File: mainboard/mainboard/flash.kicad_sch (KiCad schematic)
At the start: 5 parts

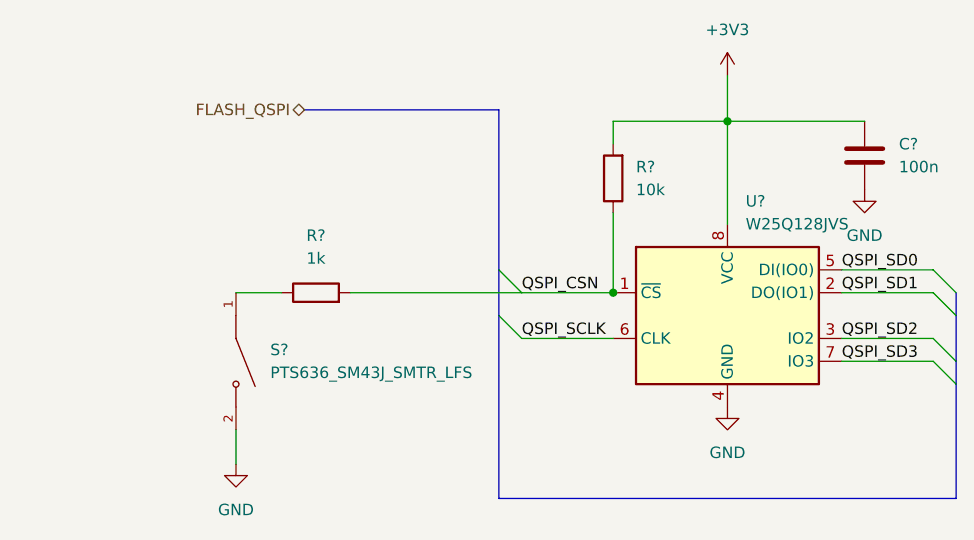
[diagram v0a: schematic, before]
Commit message: Fixing labels
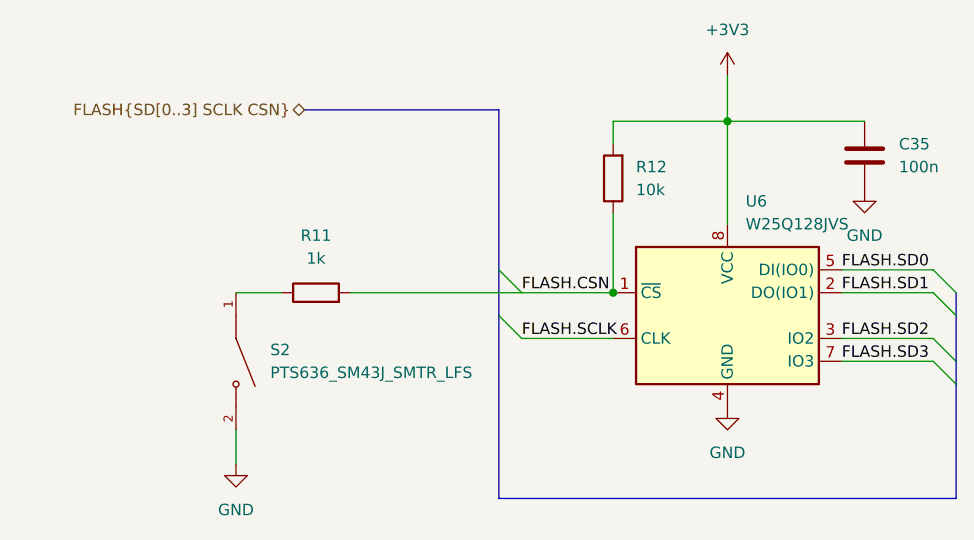
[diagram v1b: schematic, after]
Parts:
- gave numbers to parts that had none: 5
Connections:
- net QSPI_CSN renamed FLASH.CSN
- net QSPI_SCLK renamed FLASH.SCLK
- net QSPI_SD0 renamed FLASH.SD0
- net QSPI_SD1 renamed FLASH.SD1
- net QSPI_SD2 renamed FLASH.SD2
- net QSPI_SD3 renamed FLASH.SD3
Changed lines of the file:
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@@
     (stroke (width 0) (type default) (color 0 0 0 0))
   )
-  (label "QSPI_CSN" (at 123.19 81.28 0)
+  (label "FLASH.CSN" (at 123.19 81.28 0)
     (effects (font (size 1.27 1.27)) (justify left bottom))
   )
-  (label "QSPI_SCLK" (at 123.19 86.36 0)
+  (label "FLASH.SCLK" (at 123.19 86.36 0)
     (effects (font (size 1.27 1.27)) (justify left bottom))
   )
-  (label "QSPI_SD3" (at 158.75 88.9 0)
+  (label "FLASH.SD3" (at 158.75 88.9 0)
     (effects (font (size 1.27 1.27)) (justify left bottom))
   )
-  (label "QSPI_SD0" (at 158.75 78.74 0)
+  (label "FLASH.SD0" (at 158.75 78.74 0)
     (effects (font (size 1.27 1.27)) (justify left bottom))
   )
-  (label "QSPI_SD1" (at 158.75 81.28 0)
+  (label "FLASH.SD1" (at 158.75 81.28 0)
     (effects (font (size 1.27 1.27)) (justify left bottom))
   )
-  (label "QSPI_SD2" (at 158.75 86.36 0)
+  (label "FLASH.SD2" (at 158.75 86.36 0)
     (effects (font (size 1.27 1.27)) (justify left bottom))
   )
-  (hierarchical_label "FLASH_QSPI" (shape bidirectional) (at 99.06 60.96 180)
+  (hierarchical_label "FLASH{SD[0..3] SCLK CSN}" (shape bidirectional) (at 99.06 60.96 180)
     (effects (font (size 1.27 1.27)) (justify right))
   )
   (symbol (lib_id "Device:R") (at 100.33 81.28 90) (unit 1)
     (in_bom yes) (on_board yes) (fields_autoplaced)
-    (property "Reference" "R?" (id 0) (at 100.33 74.93 90))
+    (property "Reference" "R11" (id 0) (at 100.33 74.93 90))
     (property "Value" "1k" (id 1) (at 100.33 77.47 90))
     (property "Footprint" "Resistor_SMD:R_0402_1005Metric_Pad0.72x0.64mm_HandSolder" (id 2) (at 100.33 83.058 90)
@@
   (symbol (lib_id "Device:R") (at 133.35 68.58 180) (unit 1)
     (in_bom yes) (on_board yes) (fields_autoplaced)
-    (property "Reference" "R?" (id 0) (at 135.89 67.3099 0)
+    (property "Reference" "R12" (id 0) (at 135.89 67.3099 0)
       (effects (font (size 1.27 1.27)) (justify right))
     )
@@
   (symbol (lib_id "power:GND") (at 146.05 93.98 0) (unit 1)
     (in_bom yes) (on_board yes) (fields_autoplaced)
-    (property "Reference" "#PWR?" (id 0) (at 146.05 100.33 0)
+    (property "Reference" "#PWR044" (id 0) (at 146.05 100.33 0)
       (effects (font (size 1.27 1.27)) hide)
     )
@@
   (symbol (lib_id "PTS636_SM43J_SMTR_LFS:PTS636_SM43J_SMTR_LFS") (at 91.44 88.9 270) (unit 1)
     (in_bom yes) (on_board yes)
-    (property "Reference" "S?" (id 0) (at 95.25 87.6299 90)
+    (property "Reference" "S2" (id 0) (at 95.25 87.6299 90)
       (effects (font (size 1.27 1.27)) (justify left))
     )
@@
   (symbol (lib_id "power:GND") (at 161.29 69.85 0) (unit 1)
     (in_bom yes) (on_board yes) (fields_autoplaced)
-    (property "Reference" "#PWR?" (id 0) (at 161.29 76.2 0)
+    (property "Reference" "#PWR045" (id 0) (at 161.29 76.2 0)
       (effects (font (size 1.27 1.27)) hide)
     )
@@
   (symbol (lib_id "power:GND") (at 91.44 100.33 0) (unit 1)
     (in_bom yes) (on_board yes) (fields_autoplaced)
-    (property "Reference" "#PWR?" (id 0) (at 91.44 106.68 0)
+    (property "Reference" "#PWR042" (id 0) (at 91.44 106.68 0)
       (effects (font (size 1.27 1.27)) hide)
     )
@@
   (symbol (lib_id "Device:C") (at 161.29 66.04 0) (unit 1)
     (in_bom yes) (on_board yes) (fields_autoplaced)
-    (property "Reference" "C?" (id 0) (at 165.1 64.7699 0)
+    (property "Reference" "C35" (id 0) (at 165.1 64.7699 0)
       (effects (font (size 1.27 1.27)) (justify left))
     )
@@
   (symbol (lib_id "Memory_Flash:W25Q128JVS") (at 146.05 83.82 0) (unit 1)
     (in_bom yes) (on_board yes) (fields_autoplaced)
-    (property "Reference" "U?" (id 0) (at 148.0694 71.12 0)
+    (property "Reference" "U6" (id 0) (at 148.0694 71.12 0)
       (effects (font (size 1.27 1.27)) (justify left))
     )
@@
   (symbol (lib_id "power:+3V3") (at 146.05 57.15 0) (unit 1)
     (in_bom yes) (on_board yes) (fields_autoplaced)
-    (property "Reference" "#PWR?" (id 0) (at 146.05 60.96 0)
+    (property "Reference" "#PWR043" (id 0) (at 146.05 60.96 0)
       (effects (font (size 1.27 1.27)) hide)
     )

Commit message: board almost ready, paths must be aligned
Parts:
- C401: renamed from C35; footprint Capacitor_SMD:C_0402_1005Metric_Pad0.74x0.62mm_HandSolder -> Capacitor_SMD:C_0603_1608Metric_Pad1.08x0.95mm_HandSolder
- R401: renamed from R11; footprint Resistor_SMD:R_0402_1005Metric_Pad0.72x0.64mm_HandSolder -> Resistor_SMD:R_0603_1608Metric_Pad0.98x0.95mm_HandSolder
- R402: renamed from R12; footprint Resistor_SMD:R_0402_1005Metric_Pad0.72x0.64mm_HandSolder -> Resistor_SMD:R_0603_1608Metric_Pad0.98x0.95mm_HandSolder
- renumbered S2 to S401, U6 to U401

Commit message: motherboard designed
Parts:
- U: renamed from R401; value 1k -> (none); footprint Resistor_SMD:R_0603_1608Metric_Pad0.98x0.95mm_HandSolder -> (none)
- U: renamed from R402; value 10k -> (none); footprint Resistor_SMD:R_0603_1608Metric_Pad0.98x0.95mm_HandSolder -> (none)
- U: renamed from S401; value PTS636_SM43J_SMTR_LFS -> (none); footprint SW_PTS636_SM43J_SMTR_LFS -> (none)
- U: renamed from C401; value 100n -> (none); footprint Capacitor_SMD:C_0603_1608Metric_Pad1.08x0.95mm_HandSolder -> (none)
- U: renamed from U401; value W25Q128JVS -> (none); footprint Package_SO:SOIC-8_5.23x5.23mm_P1.27mm -> (none)
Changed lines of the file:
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@@
-(kicad_sch (version 20220104) (generator eeschema)
+(kicad_sch (version 20220404) (generator eeschema)
   (paper "A4")
   (junction (at 146.05 62.23) (diameter 0) (color 0 0 0 0)
@@
   (symbol (lib_id "Device:R") (at 100.33 81.28 90) (unit 1)
     (in_bom yes) (on_board yes) (fields_autoplaced)
-    (property "Reference" "R401" (id 0) (at 100.33 74.93 90)
-      (effects (font (size 1.27 1.27)))
-    )
-    (property "Value" "1k" (id 1) (at 100.33 77.47 90)
-      (effects (font (size 1.27 1.27)))
-    )
-    (property "Footprint" "Resistor_SMD:R_0603_1608Metric_Pad0.98x0.95mm_HandSolder" (id 2) (at 100.33 83.058 90)
+    (default_instance (reference "U") (unit 1) (value "") (footprint ""))
+    (property "Reference" "U" (id 0) (at 100.33 74.93 90)
+      (effects (font (size 1.27 1.27)))
+    )
+    (property "Value" "" (id 1) (at 100.33 77.47 90)
+      (effects (font (size 1.27 1.27)))
+    )
+    (property "Footprint" "" (id 2) (at 100.33 83.058 90)
       (effects (font (size 1.27 1.27)) hide)
     )
@@
   (symbol (lib_id "Device:R") (at 133.35 68.58 180) (unit 1)
     (in_bom yes) (on_board yes) (fields_autoplaced)
-    (property "Reference" "R402" (id 0) (at 135.89 67.3099 0)
+    (default_instance (reference "U") (unit 1) (value "") (footprint ""))
+    (property "Reference" "U" (id 0) (at 135.89 67.3099 0)
       (effects (font (size 1.27 1.27)) (justify right))
     )
-    (property "Value" "10k" (id 1) (at 135.89 69.8499 0)
+    (property "Value" "" (id 1) (at 135.89 69.8499 0)
       (effects (font (size 1.27 1.27)) (justify right))
     )
-    (property "Footprint" "Resistor_SMD:R_0603_1608Metric_Pad0.98x0.95mm_HandSolder" (id 2) (at 135.128 68.58 90)
+    (property "Footprint" "" (id 2) (at 135.128 68.58 90)
       (effects (font (size 1.27 1.27)) hide)
     )
@@
   (symbol (lib_id "power:GND") (at 146.05 93.98 0) (unit 1)
     (in_bom yes) (on_board yes) (fields_autoplaced)
-    (property "Reference" "#PWR0403" (id 0) (at 146.05 100.33 0)
-      (effects (font (size 1.27 1.27)) hide)
-    )
-    (property "Value" "GND" (id 1) (at 146.05 99.06 0)
+    (default_instance (reference "U") (unit 1) (value "") (footprint ""))
+    (property "Reference" "U" (id 0) (at 146.05 100.33 0)
+      (effects (font (size 1.27 1.27)) hide)
+    )
+    (property "Value" "" (id 1) (at 146.05 99.06 0)
       (effects (font (size 1.27 1.27)))
     )
@@
   (symbol (lib_id "PTS636_SM43J_SMTR_LFS:PTS636_SM43J_SMTR_LFS") (at 91.44 88.9 270) (unit 1)
     (in_bom yes) (on_board yes)
-    (property "Reference" "S401" (id 0) (at 95.25 87.6299 90)
-      (effects (font (size 1.27 1.27)) (justify left))
-    )
-    (property "Value" "PTS636_SM43J_SMTR_LFS" (id 1) (at 95.25 90.17 90)
-      (effects (font (size 1.27 1.27)) (justify left))
-    )
-    (property "Footprint" "SW_PTS636_SM43J_SMTR_LFS" (id 2) (at 91.44 88.9 0)
+    (default_instance (reference "U") (unit 1) (value "") (footprint ""))
+    (property "Reference" "U" (id 0) (at 95.25 87.6299 90)
+      (effects (font (size 1.27 1.27)) (justify left))
+    )
+    (property "Value" "" (id 1) (at 95.25 90.17 90)
+      (effects (font (size 1.27 1.27)) (justify left))
+    )
+    (property "Footprint" "" (id 2) (at 91.44 88.9 0)
       (effects (font (size 1.27 1.27)) (justify left bottom) hide)
     )
@@
   (symbol (lib_id "power:GND") (at 161.29 69.85 0) (unit 1)
     (in_bom yes) (on_board yes) (fields_autoplaced)
-    (property "Reference" "#PWR0404" (id 0) (at 161.29 76.2 0)
-      (effects (font (size 1.27 1.27)) hide)
-    )
-    (property "Value" "GND" (id 1) (at 161.29 74.93 0)
+    (default_instance (reference "U") (unit 1) (value "") (footprint ""))
+    (property "Reference" "U" (id 0) (at 161.29 76.2 0)
+      (effects (font (size 1.27 1.27)) hide)
+    )
+    (property "Value" "" (id 1) (at 161.29 74.93 0)
       (effects (font (size 1.27 1.27)))
     )
@@
   (symbol (lib_id "power:GND") (at 91.44 100.33 0) (unit 1)
     (in_bom yes) (on_board yes) (fields_autoplaced)
-    (property "Reference" "#PWR0401" (id 0) (at 91.44 106.68 0)
-      (effects (font (size 1.27 1.27)) hide)
-    )
-    (property "Value" "GND" (id 1) (at 91.44 105.41 0)
+    (default_instance (reference "U") (unit 1) (value "") (footprint ""))
+    (property "Reference" "U" (id 0) (at 91.44 106.68 0)
+      (effects (font (size 1.27 1.27)) hide)
+    )
+    (property "Value" "" (id 1) (at 91.44 105.41 0)
       (effects (font (size 1.27 1.27)))
     )
@@
   (symbol (lib_id "Device:C") (at 161.29 66.04 0) (unit 1)
     (in_bom yes) (on_board yes) (fields_autoplaced)
-    (property "Reference" "C401" (id 0) (at 165.1 64.7699 0)
-      (effects (font (size 1.27 1.27)) (justify left))
-    )
-    (property "Value" "100n" (id 1) (at 165.1 67.3099 0)
-      (effects (font (size 1.27 1.27)) (justify left))
-    )
-    (property "Footprint" "Capacitor_SMD:C_0603_1608Metric_Pad1.08x0.95mm_HandSolder" (id 2) (at 162.2552 69.85 0)
+    (default_instance (reference "U") (unit 1) (value "") (footprint ""))
+    (property "Reference" "U" (id 0) (at 165.1 64.7699 0)
+      (effects (font (size 1.27 1.27)) (justify left))
+    )
+    (property "Value" "" (id 1) (at 165.1 67.3099 0)
+      (effects (font (size 1.27 1.27)) (justify left))
+    )
+    (property "Footprint" "" (id 2) (at 162.2552 69.85 0)
       (effects (font (size 1.27 1.27)) hide)
     )
@@
   (symbol (lib_id "Memory_Flash:W25Q128JVS") (at 146.05 83.82 0) (unit 1)
     (in_bom yes) (on_board yes) (fields_autoplaced)
-    (property "Reference" "U401" (id 0) (at 148.0694 71.12 0)
-      (effects (font (size 1.27 1.27)) (justify left))
-    )
-    (property "Value" "W25Q128JVS" (id 1) (at 148.0694 73.66 0)
-      (effects (font (size 1.27 1.27)) (justify left))
-    )
-    (property "Footprint" "Package_SO:SOIC-8_5.23x5.23mm_P1.27mm" (id 2) (at 146.05 83.82 0)
+    (default_instance (reference "U") (unit 1) (value "") (footprint ""))
+    (property "Reference" "U" (id 0) (at 148.0694 71.12 0)
+      (effects (font (size 1.27 1.27)) (justify left))
+    )
+    (property "Value" "" (id 1) (at 148.0694 73.66 0)
+      (effects (font (size 1.27 1.27)) (justify left))
+    )
+    (property "Footprint" "" (id 2) (at 146.05 83.82 0)
       (effects (font (size 1.27 1.27)) hide)
     )
@@
   (symbol (lib_id "power:+3V3") (at 146.05 57.15 0) (unit 1)
     (in_bom yes) (on_board yes) (fields_autoplaced)
-    (property "Reference" "#PWR0402" (id 0) (at 146.05 60.96 0)
-      (effects (font (size 1.27 1.27)) hide)
-    )
-    (property "Value" "+3V3" (id 1) (at 146.05 52.07 0)
-      (effects (font (size 1.27 1.27)))
-    )
+    (default_instance (reference "U") (unit 1) (value "") (footprint ""))
+    (property "Reference" "U" (id 0) (at 146.05 60.96 0)
+      (effects (font (size 1.27 1.27)) hide)
+    )
+    (property "Value" "" (id 1) (at 146.05 52.07 0)
+      (effects (font (size 1.27 1.27)))
+    )

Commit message: schematic for gpu extension
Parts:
- C401: renamed from U; value (none) -> 100n; footprint (none) -> Capacitor_SMD:C_0603_1608Metric_Pad1.08x0.95mm_HandSolder
- R401: renamed from U; value (none) -> 1k; footprint (none) -> Resistor_SMD:R_0603_1608Metric_Pad0.98x0.95mm_HandSolder
- R402: renamed from U; value (none) -> 10k; footprint (none) -> Resistor_SMD:R_0603_1608Metric_Pad0.98x0.95mm_HandSolder
- S401: renamed from U; value (none) -> PTS636_SM43J_SMTR_LFS; footprint (none) -> footprints:SW_PTS636_SM43J_SMTR_LFS
- U401: renamed from U; value (none) -> W25Q128JVS; footprint (none) -> Package_SO:SOIC-8_5.23x5.23mm_P1.27mm

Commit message: some ERC fixes
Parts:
- S401: footprint footprints:SW_PTS636_SM43J_SMTR_LFS -> SW_PTS636_SM43J_SMTR_LFS
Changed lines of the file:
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@@
       (effects (font (size 1.27 1.27)) (justify left))
     )
-    (property "Footprint" "footprints:SW_PTS636_SM43J_SMTR_LFS" (at 91.44 88.9 0)
+    (property "Footprint" "SW_PTS636_SM43J_SMTR_LFS" (at 91.44 88.9 0)
       (effects (font (size 1.27 1.27)) (justify left bottom) hide)
     )
@@
       (project "mainboard"
         (path "/e63e39d7-6ac0-4ffd-8aa3-1841a4541b55/9cc1db10-8093-47b8-8876-8e0be9b45cae"
-          (reference "S401") (unit 1) (value "PTS636_SM43J_SMTR_LFS") (footprint "footprints:SW_PTS636_SM43J_SMTR_LFS")
+          (reference "S401") (unit 1) (value "PTS636_SM43J_SMTR_LFS") (footprint "SW_PTS636_SM43J_SMTR_LFS")
         )
       )

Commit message: gpu and motherboard passes tests, now time for fpga
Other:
- title: (none) -> MSPC
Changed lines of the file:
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@@
 (kicad_sch (version 20221004) (generator eeschema)
   (paper "A4")
+  (title_block
+    (title "MSPC")
+    (rev "1")
+  )
   (junction (at 146.05 62.23) (diameter 0) (color 0 0 0 0)
   )

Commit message: refactored mainboard schematic
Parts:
- removed C401: 100n, Capacitor_SMD:C_0603_1608Metric_Pad1.08x0.95mm_HandSolder, symbol Device:C
- removed R401: 1k, Resistor_SMD:R_0603_1608Metric_Pad0.98x0.95mm_HandSolder, symbol Device:R
- removed R402: 10k, Resistor_SMD:R_0603_1608Metric_Pad0.98x0.95mm_HandSolder, symbol Device:R
- removed S401: PTS636_SM43J_SMTR_LFS, SW_PTS636_SM43J_SMTR_LFS, symbol PTS636_SM43J_SMTR_LFS:PTS636_SM43J_SMTR_LFS
- removed U401: W25Q128JVS, Package_SO:SOIC-8_5.23x5.23mm_P1.27mm, symbol Memory_Flash:W25Q128JVS
